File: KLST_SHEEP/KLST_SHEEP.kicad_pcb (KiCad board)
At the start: 4 copper layers, 100 x 100 mm, 136 parts, among them J1 Micro_SD_Card_Card_Detect_SPI, J10 LINE_IN, J11 LINE_OUT, J12 UART_00, J13 I2C_00+SPI_00, J14 UART_01, J15 GMT028-05_V1.1, J2 GPIO+AUDIO+ANALOG, J3 USB_A, J4 GPIO_EXT_A, J5 USB_B_Micro, J6 GPIO_EXT_B, J7 GPIO_EXT_C, J8 ARM_JTAG_SWD(STDC14), J9 HEADPHONES+MIC, Q1 AO3401A, SW1 BUTTON_BOOT_FLASH, SW2 BUTTON_RESET, SW3 ENCODER, SW4 ENCODER, SW6 BUTTON, U1 STM32H743VITx, U2 AMS1117-3.3, U3 WM8731SEDS, X1 KLST_SHEEP--graphics, X2 KLST_SHEEP--icon, Y1 16MHz

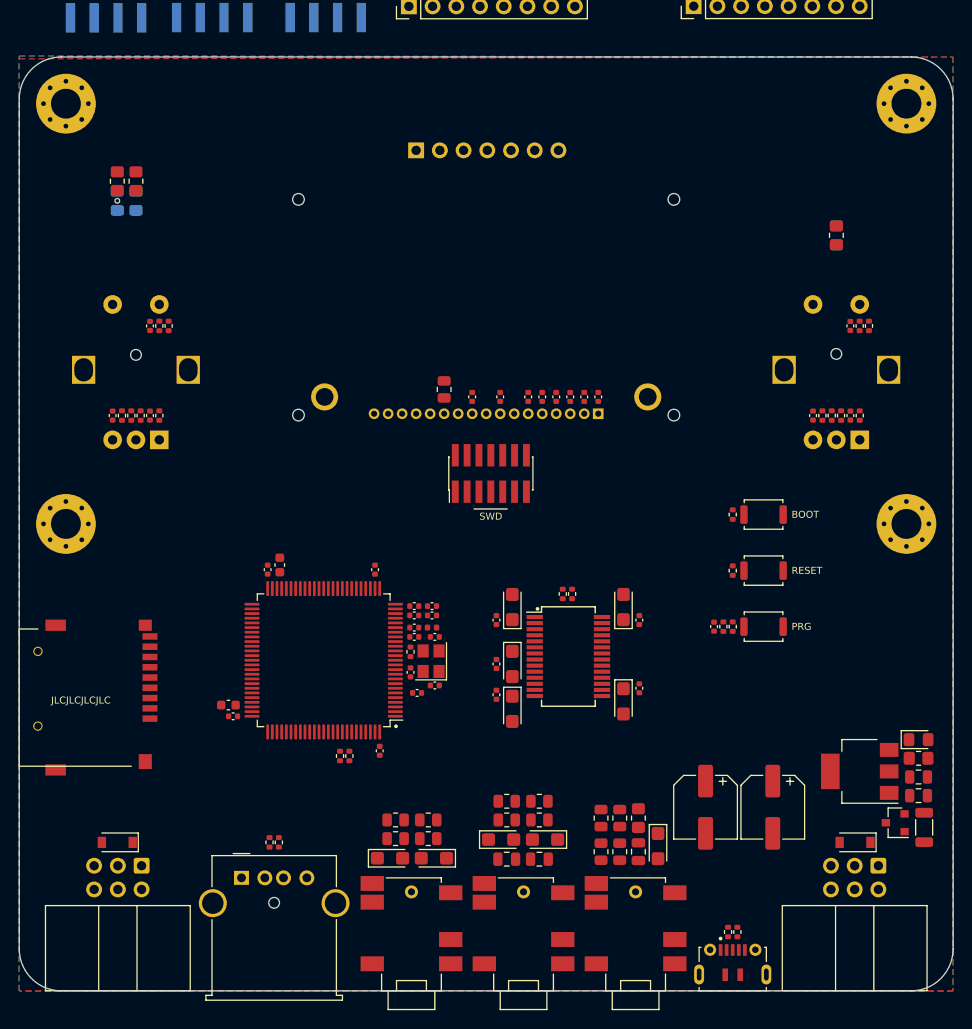
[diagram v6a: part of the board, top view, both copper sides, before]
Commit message: added icons
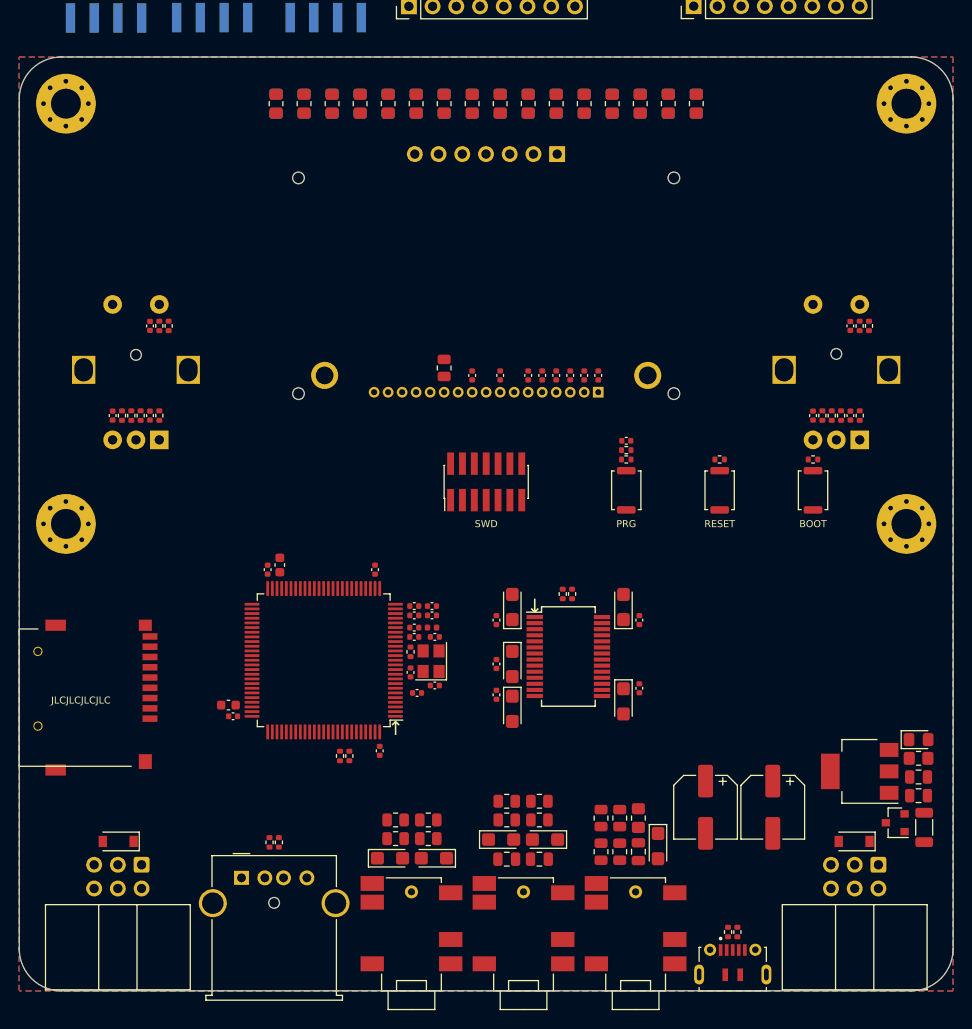
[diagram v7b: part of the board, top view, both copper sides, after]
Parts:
- removed the J12 at (93.1, 136.6)
- removed the J14 at (172.0, 136.6)
- added D10: LED, LED_SMD:LED_0805_2012Metric_Pad1.15x1.40mm_HandSolder, B.Cu at (131.5, 55.0)
- added D11: LED, LED_SMD:LED_0805_2012Metric_Pad1.15x1.40mm_HandSolder, B.Cu at (134.5, 55.0)
- added D12: LED, LED_SMD:LED_0805_2012Metric_Pad1.15x1.40mm_HandSolder, B.Cu at (137.5, 55.0)
- added D13: LED, LED_SMD:LED_0805_2012Metric_Pad1.15x1.40mm_HandSolder, B.Cu at (140.5, 55.0)
- added D14: LED, LED_SMD:LED_0805_2012Metric_Pad1.15x1.40mm_HandSolder, B.Cu at (143.5, 55.0)
- added D15: LED, LED_SMD:LED_0805_2012Metric_Pad1.15x1.40mm_HandSolder, B.Cu at (146.5, 55.0)
- added D16: LED, LED_SMD:LED_0805_2012Metric_Pad1.15x1.40mm_HandSolder, B.Cu at (149.5, 55.0)
- added D17: LED, LED_SMD:LED_0805_2012Metric_Pad1.15x1.40mm_HandSolder, B.Cu at (152.5, 55.0)
- added D18: D_Schottky, Diode_SMD:D_SOD-123, F.Cu at (169.4, 134.0)
- added D19: D_Schottky, Diode_SMD:D_SOD-123, F.Cu at (90.6, 134.0)
- added D4: LED, LED_SMD:LED_0805_2012Metric_Pad1.15x1.40mm_HandSolder, B.Cu at (116.5, 55.0)
- added D7: LED, LED_SMD:LED_0805_2012Metric_Pad1.15x1.40mm_HandSolder, B.Cu at (125.5, 55.0)
- added D8: LED, LED_SMD:LED_0805_2012Metric_Pad1.15x1.40mm_HandSolder, B.Cu at (128.5, 55.0)
- added J13: UART_00, Connector_IDC:IDC-Header_2x03_P2.54mm_Horizontal, F.Cu at (172.0, 136.5)
- added J15: UART_01, Connector_IDC:IDC-Header_2x03_P2.54mm_Horizontal, F.Cu at (93.1, 136.5)
- added R10: 1K, Resistor_SMD:R_0805_2012Metric_Pad1.20x1.40mm_HandSolder, F.Cu at (122.5, 55.0)
- added R11: 1K, Resistor_SMD:R_0805_2012Metric_Pad1.20x1.40mm_HandSolder, F.Cu at (125.5, 55.0)
- added R16: 1K, Resistor_SMD:R_0805_2012Metric_Pad1.20x1.40mm_HandSolder, F.Cu at (131.5, 55.0)
- added R17: 1K, Resistor_SMD:R_0805_2012Metric_Pad1.20x1.40mm_HandSolder, F.Cu at (134.5, 55.0)
- added R18: 1K, Resistor_SMD:R_0805_2012Metric_Pad1.20x1.40mm_HandSolder, F.Cu at (137.5, 55.0)
- added R19: 1K, Resistor_SMD:R_0805_2012Metric_Pad1.20x1.40mm_HandSolder, F.Cu at (140.5, 55.0)
- added R20: 1K, Resistor_SMD:R_0805_2012Metric_Pad1.20x1.40mm_HandSolder, F.Cu at (143.5, 55.0)
- added R21: 1K, Resistor_SMD:R_0805_2012Metric_Pad1.20x1.40mm_HandSolder, F.Cu at (146.5, 55.0)
- added R22: 1K, Resistor_SMD:R_0805_2012Metric_Pad1.20x1.40mm_HandSolder, F.Cu at (149.5, 55.0)
- added R23: 1K, Resistor_SMD:R_0805_2012Metric_Pad1.20x1.40mm_HandSolder, F.Cu at (152.5, 55.0)
- added R25: 30R, Resistor_SMD:R_0805_2012Metric, F.Cu at (125.5, 83.3)
- added R8: 1K, Resistor_SMD:R_0805_2012Metric_Pad1.20x1.40mm_HandSolder, F.Cu at (116.5, 55.0)
- added R9: 1K, Resistor_SMD:R_0805_2012Metric_Pad1.20x1.40mm_HandSolder, F.Cu at (119.5, 55.0)
- added X3: KLST_SHEEP--wolf, KLST_SHEEP:KLST_SHEEP--wolf, B.Cu at (130.0, 115.0)
- D5, D6: value D_Schottky -> LED; footprint Diode_SMD:D_SOD-123 -> LED_SMD:LED_0805_2012Metric_Pad1.15x1.40mm_HandSolder; moved to B.Cu
- R12: value 30R -> 1K; footprint Resistor_SMD:R_0805_2012Metric -> Resistor_SMD:R_0805_2012Metric_Pad1.20x1.40mm_HandSolder
- X1: footprint KLST_SHEEP:KLST_SHEEP--graphics -> KLST_SHEEP:KLST--icon
- moved D6 92.0 mm to (122.5, 55.0), turned to 270 degrees
- moved D5 84.2 mm to (119.5, 55.0), turned to 270 degrees
- moved X2 75.4 mm to (92.4, 115.0)
- moved X1 74.3 mm to (167.5, 114.7), turned to 135 degrees
- moved D2 58.7 mm to (110.5, 55.0)
- moved R6 58.7 mm to (110.5, 55.0)
- moved R12 30.7 mm to (128.5, 55.0), turned to 90 degrees
- moved D3 23.4 mm to (113.5, 55.0)
- moved R7 22.6 mm to (113.5, 55.0)
- moved C53 22.0 mm to (145.0, 91.1), turned to 180 degrees
- moved R56 21.6 mm to (145.0, 92.1), turned to 180 degrees
- moved R55 21.2 mm to (145.0, 93.1), turned to 0 degrees
- moved SW5 20.7 mm to (145.0, 96.4), turned to 270 degrees
- moved D1 19.9 mm to (107.5, 55.0)
- moved R5 18.9 mm to (107.5, 55.0)
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- renumbered C56 to C53, D4 to D9, J9 to J10, J10 to J11, J11 to J12, J13 to J14, J15 to J8, J8 to J9, R8 to R13, R9 to R14, R10 to R15, R11 to R24, R13 to R26, R14 to R27, R15 to R28, R16 to R29, R17 to R30, R18 to R31, R19 to R32, R20 to R33, R21 to R34, R22 to R35, R23 to R36, R24 to R37, R25 to R38, R26 to R39, R27 to R40, R28 to R41, R29 to R42, R30 to R43, R31 to R44, R32 to R45, R33 to R46, R34 to R47, R35 to R48, R36 to R49, R37 to R50, R38 to R51, R39 to R52, R46 to R53, R47 to R54, R48 to R55, R49 to R56, SW6 to SW5
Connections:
- net /GPIO_EXT_A_02 renamed /SPI_DISPLAY_RESET
- net /GPIO_EXT_A_03 renamed /SPI_DISPLAY_REGISTER_SELECT
- net /GPIO_EXT_A_04 renamed /SPI_DISPLAY_MOSI
- net /GPIO_EXT_A_06 renamed /SPI_DISPLAY_SCK
- net /GPIO_EXT_A_07 renamed /SPI_DISPLAY_CS
- D5 pad 1: +3V3 -> Net-(D5-Pad1)
- D5 pad 2: Net-(D5-Pad2) -> (no net)
- D6 pad 1: +3V3 -> Net-(D6-Pad1)
- D6 pad 2: Net-(D6-Pad2) -> (no net)
- R12 pad 1: Net-(DS1-PadA) -> GND
- R12 pad 2: +3V3 -> Net-(D8-Pad1)
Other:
- outline, holes or cut-outs redrawn
- board text added: "SERIAL 00"
- board text added: "SERIAL 01"
- board text added: "↑"

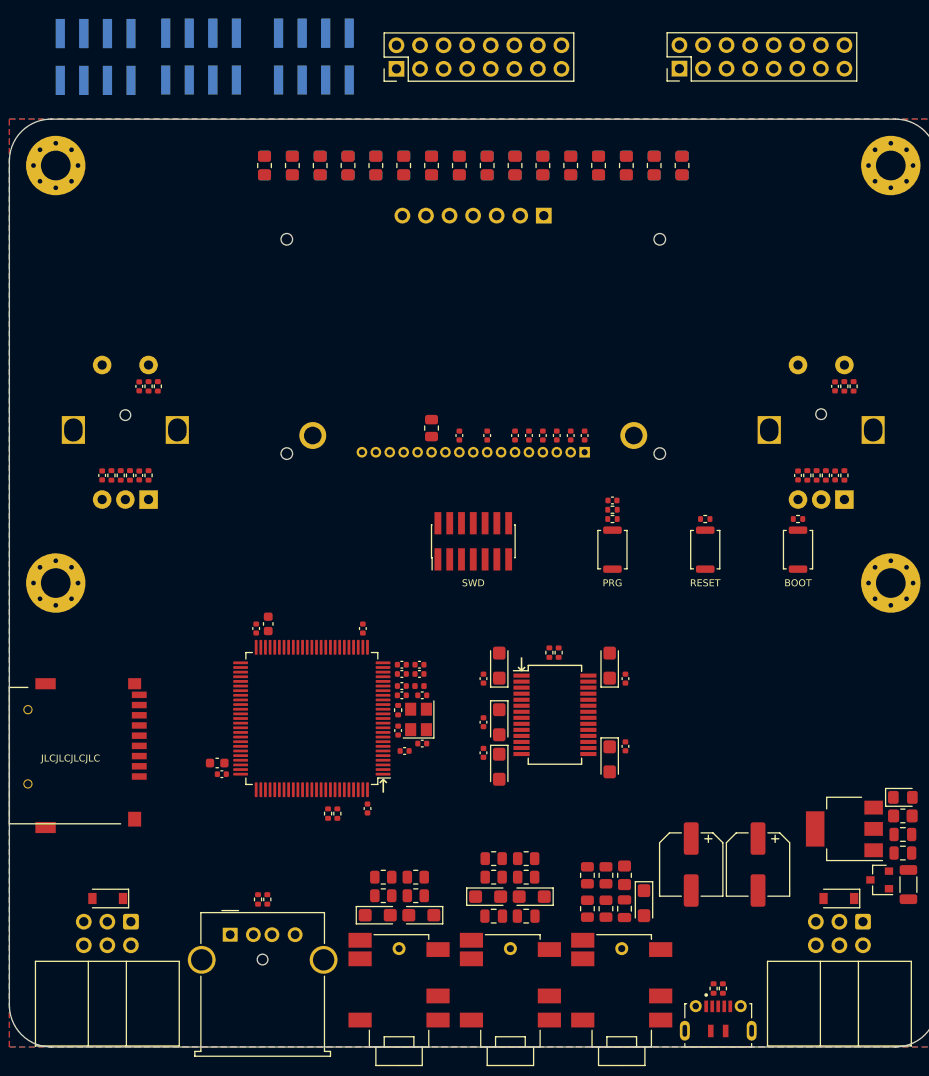
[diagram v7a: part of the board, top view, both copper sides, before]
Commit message: finished PIN assignment, cleaned up silkscreen
READY TO ROUTE :)
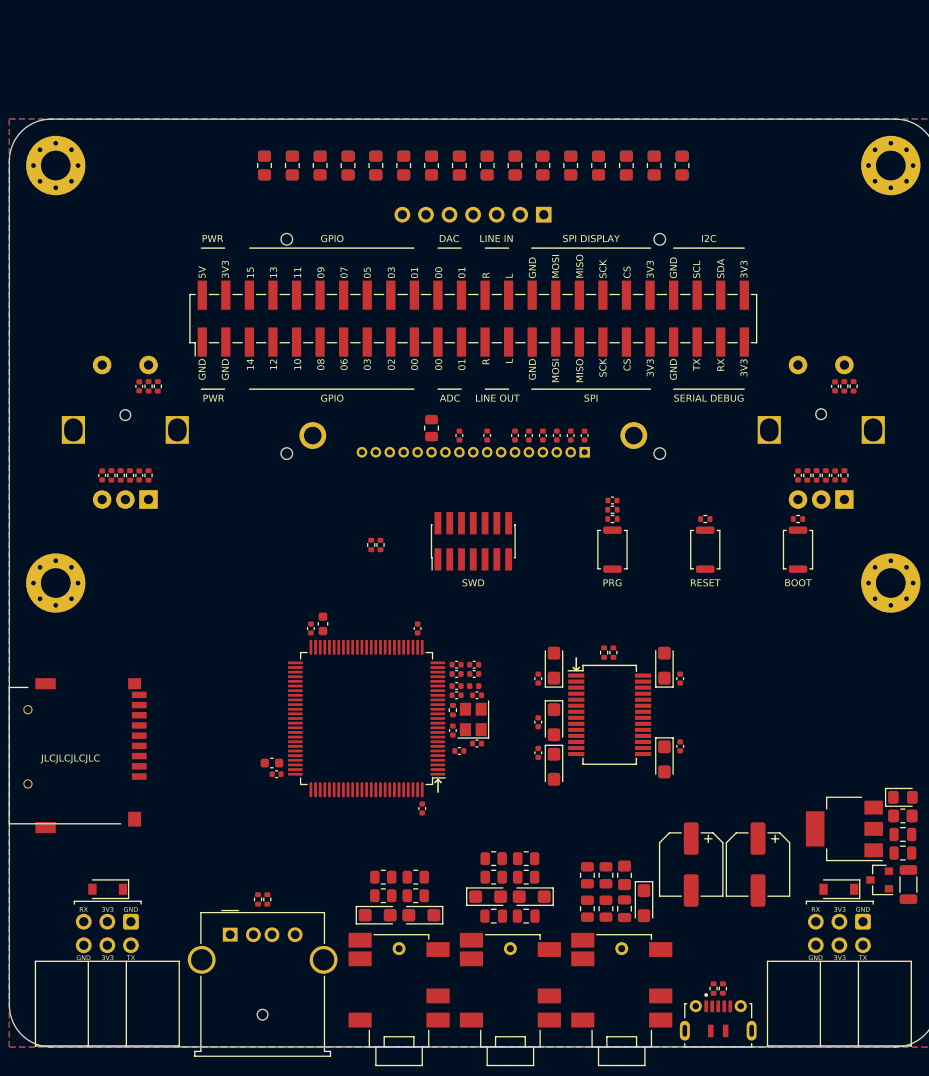
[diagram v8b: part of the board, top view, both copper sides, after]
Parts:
- removed J14: I2C_00+SPI_00, Connector_PinHeader_2.54mm:PinHeader_2x08_P2.54mm_Vertical
- removed J4: GPIO_EXT_A, Connector_PinHeader_2.54mm:PinHeader_2x04_P2.54mm_Vertical_SMD
- removed J6: GPIO_EXT_B, Connector_PinHeader_2.54mm:PinHeader_2x04_P2.54mm_Vertical_SMD
- removed J7: GPIO_EXT_C, Connector_PinHeader_2.54mm:PinHeader_2x04_P2.54mm_Vertical_SMD
- J2: value GPIO+AUDIO+ANALOG -> PERIPHERALS; footprint Connector_PinHeader_2.54mm:PinHeader_2x08_P2.54mm_Vertical -> Connector_PinHeader_2.54mm:PinHeader_2x24_P2.54mm_Vertical_SMD
- moved R53 29.3 mm to (119.0, 95.9), turned to 270 degrees
- moved R54 29.3 mm to (120.0, 95.9), turned to 270 degrees
- moved J2 28.2 mm to (130.0, 71.5)
- moved C1 5.90 mm to (130.4, 117.3)
- moved C2 5.90 mm to (130.4, 112.1)
- moved C20 5.90 mm to (128.5, 118.1)
- moved C21 5.90 mm to (124.0, 104.9)
- moved C23 5.90 mm to (112.5, 104.9)
- moved C25 5.90 mm to (124.5, 124.3)
- moved C31 5.90 mm to (150.6, 119.0)
- moved C32 5.90 mm to (152.3, 117.6)
- moved C39 5.90 mm to (137.0, 115.0)
- moved C41 5.90 mm to (137.0, 118.3)
- moved C43 5.90 mm to (152.3, 110.3)
- moved C44 5.90 mm to (150.6, 108.9)
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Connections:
- net /GPIO_EXT_C_06 renamed /BUTTON_PRG
- D10 pad 2: (no net) -> /LED_08
- D11 pad 2: (no net) -> /LED_09
- D12 pad 2: (no net) -> /LED_10
- D13 pad 2: (no net) -> /LED_11
- D14 pad 2: (no net) -> /LED_12
- D15 pad 2: (no net) -> /LED_13
- D16 pad 2: (no net) -> /LED_14
- D17 pad 2: (no net) -> /LED_15
- D4 pad 2: (no net) -> /LED_03
- D5 pad 2: (no net) -> /LED_04
- D6 pad 2: (no net) -> /LED_05
- D7 pad 2: (no net) -> /LED_06
- D8 pad 2: (no net) -> /LED_07
- J2 pad 1: /LINE_IN_RIGHT -> GND
- J2 pad 10: /GPIO_01 -> /GPIO_11
- J2 pad 11: /GPIO_02 -> /GPIO_08
- J2 pad 12: /GPIO_03 -> /GPIO_09
- J2 pad 13: /GPIO_04 -> /GPIO_06
- J2 pad 14: /GPIO_05 -> /GPIO_07
- J2 pad 15: /GPIO_06 -> /GPIO_04
- J2 pad 16: /GPIO_07 -> /GPIO_05
- J2 pad 2: /LINE_IN_LEFT -> +5V
- J2 pad 3: /LINE_OUT_RIGHT -> GND
- J2 pad 4: /LINE_OUT_LEFT -> +3V3
- J2 pad 5: /DAC_00 -> /GPIO_14
- J2 pad 6: /DAC_01 -> /GPIO_15
- J2 pad 7: /ADC_00 -> /GPIO_12
- J2 pad 8: /ADC_01 -> /GPIO_13
- J2 pad 9: /GPIO_00 -> /GPIO_10
- R53 pad 2: /I2C_00_SCL -> /I2C_USR_SDA
- R54 pad 2: /I2C_00_SDA -> /I2C_USR_SCL
- U1 pad 15: /GPIO_EXT_C_02 -> /GPIO_12
- U1 pad 24: /LED_02 -> /LED_15
- U1 pad 30: /LED_00 -> /LED_14
- U1 pad 31: /LED_01 -> /LED_13
- U1 pad 34: /GPIO_EXT_C_01 -> /LED_12
- U1 pad 35: /GPIO_EXT_C_00 -> /LED_11
- U1 pad 36: /GPIO_EXT_B_07 -> /GPIO_11
- U1 pad 39: /GPIO_EXT_B_06 -> /GPIO_10
- U1 pad 40: /GPIO_EXT_B_05 -> /GPIO_09
- U1 pad 41: /SPI_00_CS -> /SPI_USR_CS
- U1 pad 42: /SPI_00_SCK -> /SPI_USR_SCK
- U1 pad 43: /SPI_00_MISO -> /SPI_USR_MISO
- U1 pad 44: /SPI_00_MOSI -> /SPI_USR_MOSI
- U1 pad 45: /GPIO_EXT_B_04 -> /GPIO_08
- U1 pad 55: /GPIO_EXT_B_03 -> /GPIO_07
- U1 pad 56: /GPIO_EXT_B_02 -> /GPIO_06
- U1 pad 57: /GPIO_EXT_B_01 -> /GPIO_05
- U1 pad 58: /GPIO_EXT_B_00 -> /GPIO_04
- U1 pad 59: /GPIO_07 -> /LED_10
- U1 pad 60: /GPIO_06 -> /LED_09
- U1 pad 61: /GPIO_05 -> /LED_08
- U1 pad 62: /GPIO_04 -> /LED_07
- U1 pad 63: /GPIO_03 -> /LED_06
- U1 pad 64: /GPIO_02 -> /LED_05
- U1 pad 65: /GPIO_01 -> /LED_04
- U1 pad 66: /GPIO_00 -> /LED_03
- U1 pad 7: /GPIO_EXT_C_05 -> /GPIO_15
- U1 pad 79: (no net) -> /SPI_DISPLAY_MISO
- U1 pad 8: /GPIO_EXT_C_04 -> /GPIO_14
- U1 pad 83: /GPIO_EXT_A_01 -> /GPIO_03
- U1 pad 84: /GPIO_EXT_A_00 -> /GPIO_02
- U1 pad 85: (no net) -> /GPIO_01
- U1 pad 88: /GPIO_EXT_C_07 -> /GPIO_00
- U1 pad 9: /GPIO_EXT_C_03 -> /GPIO_13
- U1 pad 90: (no net) -> /LED_02
- U1 pad 91: (no net) -> /LED_01
- U1 pad 92: /I2C_00_SCL -> /I2C_USR_SCL
- U1 pad 93: /I2C_00_SDA -> /I2C_USR_SDA
- U1 pad 95: (no net) -> /LED_00
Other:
- outline, holes or cut-outs redrawn
- board text added: "08"
- board text added: "09"
- board text added: "10"
- board text added: "11"
- board text added: "12"
- board text added: "13"
- board text added: "14"
- board text added: "15"
- board text added: "LINE IN"
- board text added: "LINE OUT"
- board text added: "SERIAL DEBUG"
- board text added: "SPI DISPLAY"
- board text removed: "04"
- board text removed: "OUPUT"
- board text removed: "SERIAL"
